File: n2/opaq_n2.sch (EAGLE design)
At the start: 40 parts, among them IC2 TS5A3157, IC3 ATSHA204_SOIC8, IC4 ACS712, IC5 ADS1100, IC6 ATMega-328, IC7 AT25F512BWIDE_5.3MM, IC8 LM2594HV, K1 62101021021, X1 16 MHz

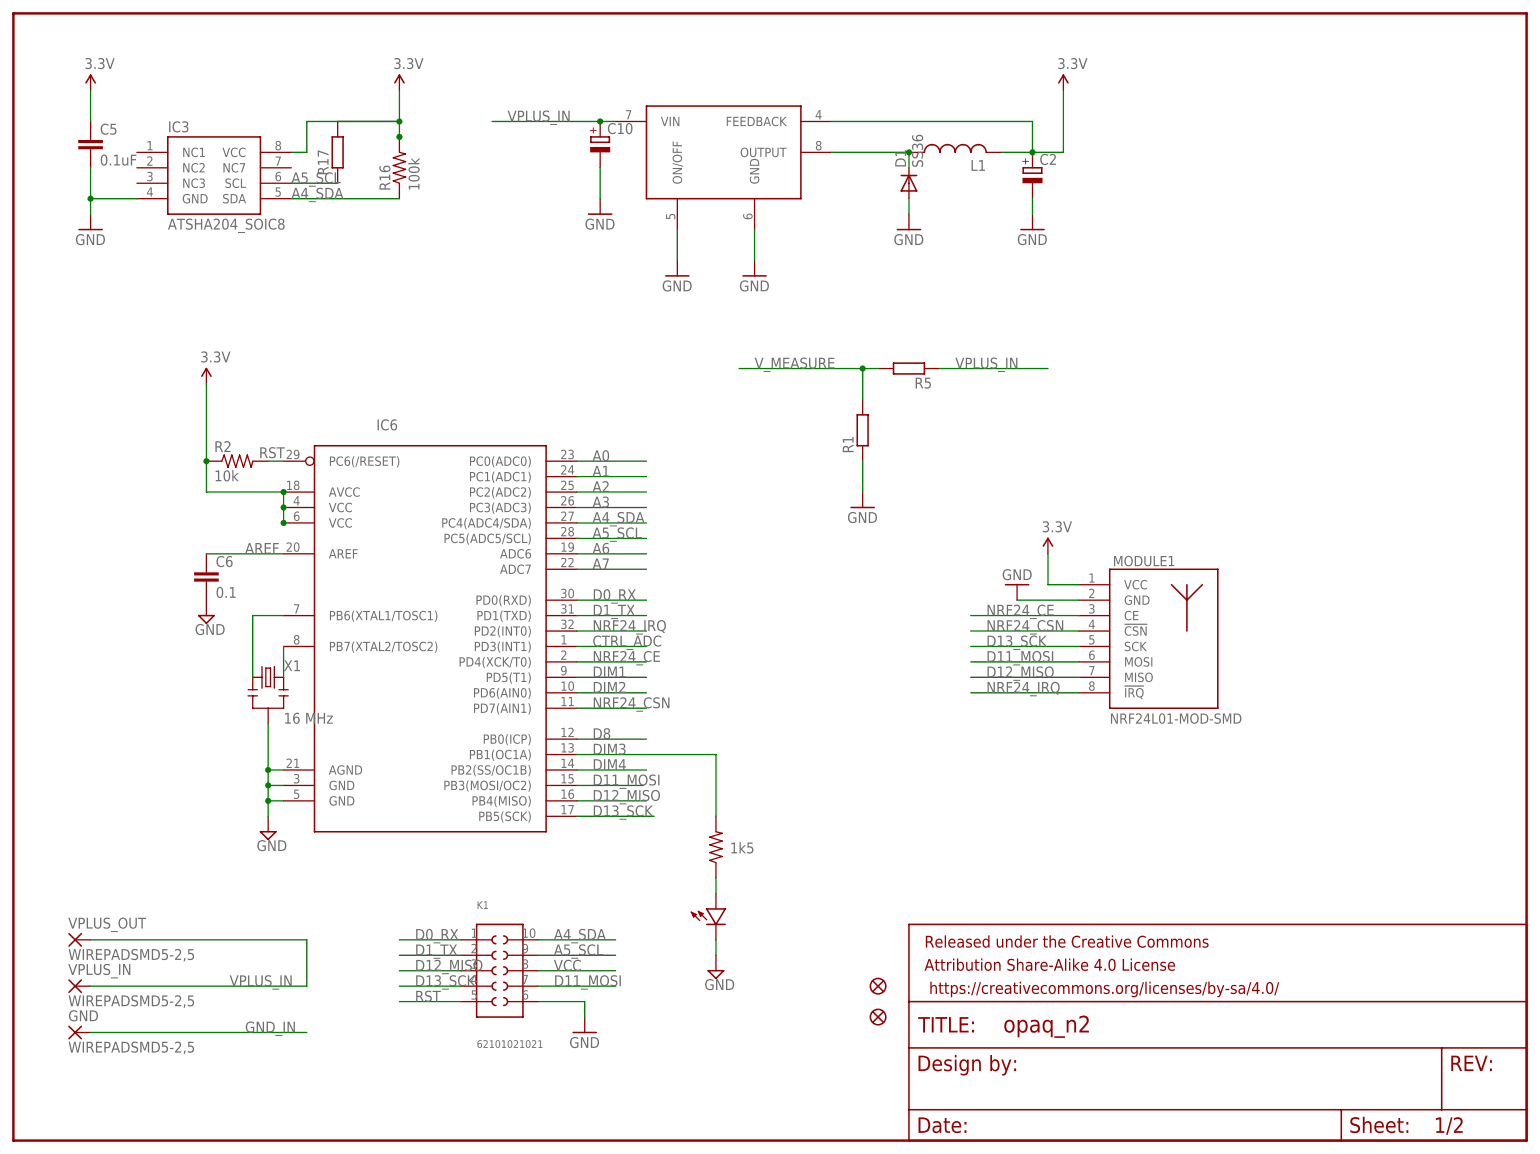
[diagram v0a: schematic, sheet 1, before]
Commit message: Updated opaq n2 hardware. Isolated power supply has been added.
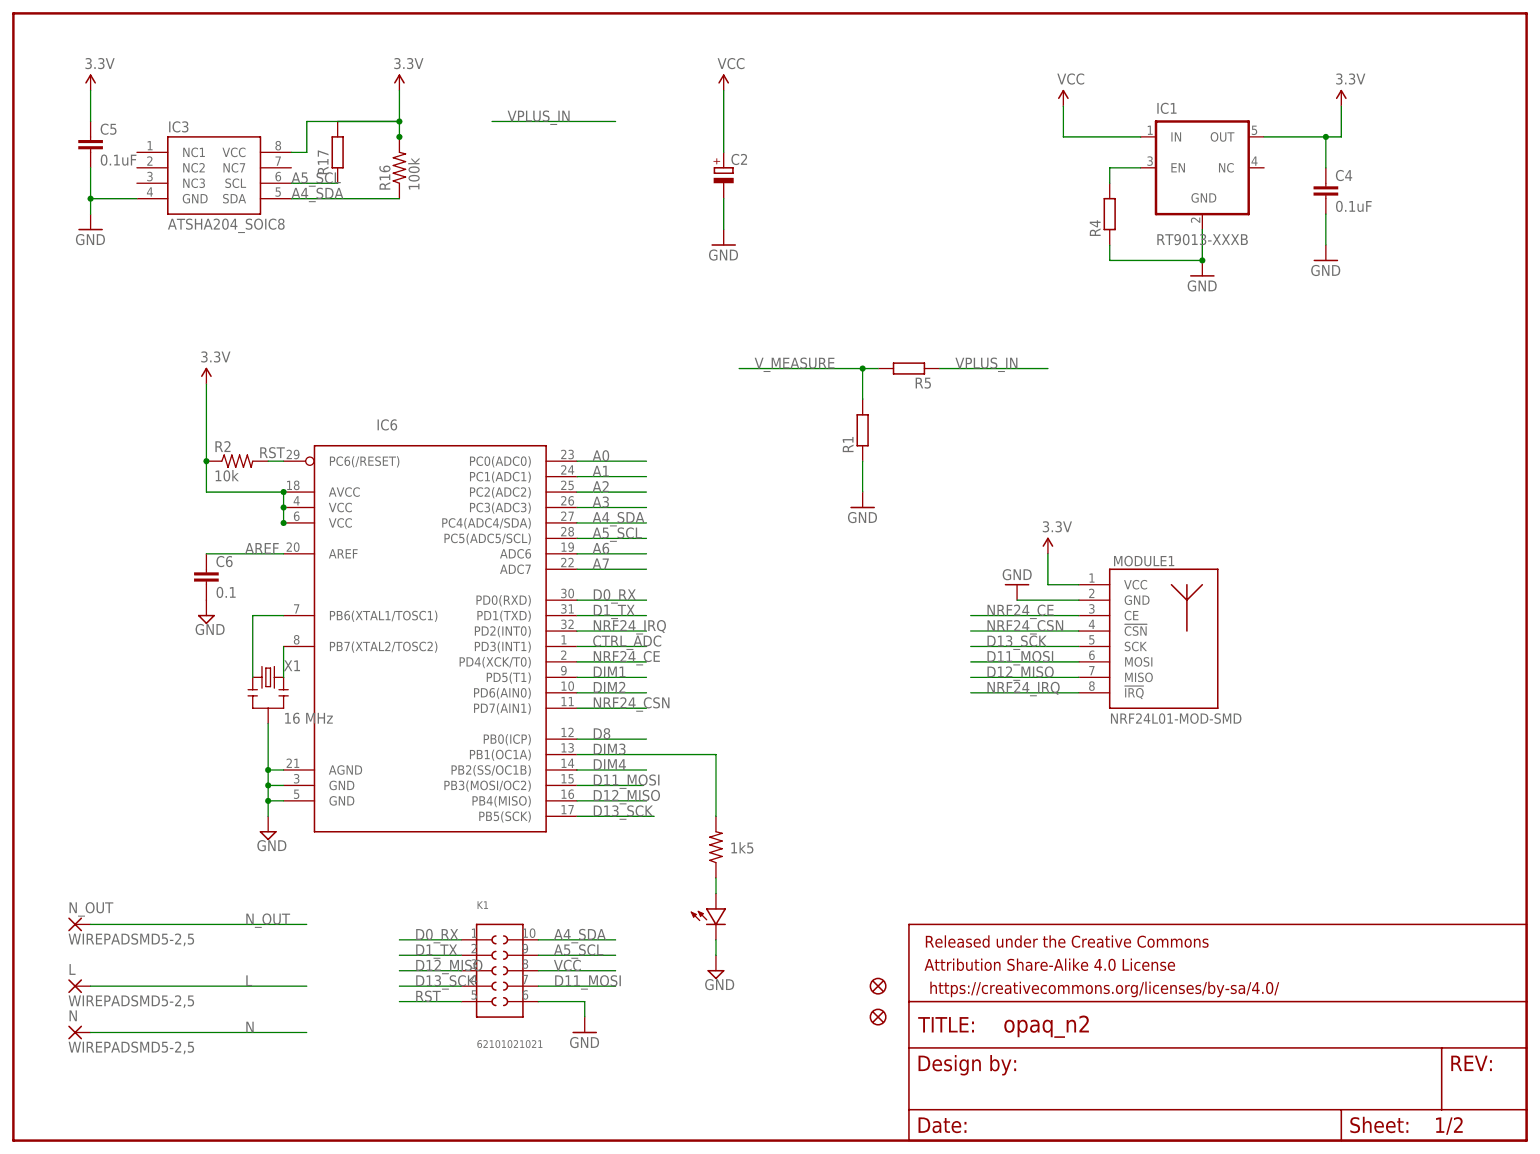
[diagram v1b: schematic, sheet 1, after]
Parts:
- removed C10: (no value), rcl:CPOL-EUD/7343-31R
- removed C8: (no value), resistor:C-EU225-062X268
- removed D1: SS36, SparkFun:DIODESMA
- removed D2, D3, D4, D5: (no value), adafruit:DIODESMA
- removed IC8: LM2594HV, apedro_lib:LM2594
- removed L1: (no value), apedro_lib:NR6045
- removed R6: (no value), resistor:R-EU_R2512W
- removed VPLUS_OUT: WIREPADSMD5-2,5, wirepad:WIREPADSMD5-2,5
- added 5V, L_IN, N_IN: MCS08, solpad:MCS08
- added C4: 0.1uF, SparkFun-Passives:CAP0805
- added IC1: RT9013-XXXB, v-reg_extra:RT9013-XXXB
- added N, N_OUT: WIREPADSMD5-2,5, wirepad:WIREPADSMD5-2,5
- added Q1: MMBT2222A, SparkFun-DiscreteSemi:TRANSISTOR_NPNMMBT2222A
- added R11, R4, R8: (no value), resistor:R-EU_R0805
- GND: value WIREPADSMD5-2,5 -> MCS08; device wirepad:WIREPADSMD5-2,5 -> solpad:MCS08
- renumbered VPLUS_IN to L
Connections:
- removed net GND_IN: GND.P, IC4.IP-@3, IC4.IP-@4
- removed net LC: C8.1, D2.C, D4.A, R6.1
- removed net N$17: D1.C, IC8.OUTPUT, L1.P$2
- removed net V+: D4.C, D5.C
- removed net V-: D2.A, D3.A
- new net N$10: IC1.EN, R4.2
- new net N_IN: IC4.IP-@3, IC4.IP-@4, U$1.NO1
- new net N_OUT: N_OUT.P, U$1.NO2
- new net RELAY_C: Q1.C, R8.2, U$1.COIL2
- new net RELAY_SET: Q1.B, R11.2
- net 3.3V: now also C4.1, IC1.OUT, R11.1; no longer C2.+, IC8.FEEDBACK, L1.P$1
- net GND: now also C4.2, GND.MP, IC1.GND, Q1.E, R4.1, U$1.COIL1; no longer C10.-, D1.A, IC4.IP+@1, IC4.IP+@2, IC8.GND, IC8.ON/OFF
- net L: now also L.P, L_IN.MP; no longer C8.2, R6.2
- net N: now also IC4.IP+@1, IC4.IP+@2, N.P, N_IN.MP; no longer D3.C, D5.A
- net VCC: now also 5V.MP, C2.+, IC1.IN, R8.1
- net VPLUS_IN: no longer C10.+, IC8.VIN, L.P, VPLUS_OUT.P
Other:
- moved on the sheet: C2

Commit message: Candidate version of opaq n2 for pcb production.
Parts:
- removed R8: (no value), resistor:R-EU_R0805
- added 7K471: (no value), ptc-ntc:B57164
- added CC: MCS08, solpad:MCS08
- added D1: tvs 5v, SparkFun:DIODESOD
- added D2: 1N4148, SparkFun:DIODESOD
- added D3: (no value), SparkFun:DIODESMB
- added R6, R7: (no value), resistor:R-EU_R0805
- added TRF250-300: (no value), fuse:TE5
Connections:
- removed net DIM1: IC6.PD5(T1)
- removed net L: L.P, L_IN.MP
- removed net RELAY_C: Q1.C, R8.2, U$1.COIL2
- new net CC: CC.MP, IC4.IP-@3, IC4.IP-@4
- new net CURRENT_VOUT5V: IC4.VOUT, R7.1
- new net LL: L.P, TRF250-300.1
- new net L_SAFE: 7K471.1, L_IN.MP
- new net N$3: 7K471.2, TRF250-300.2
- new net RELAY_GND: D2.A, Q1.C, U$1.COIL1
- net 3.3V: now also K1.8; no longer IC4.VCC
- net CURRENT_VOUT: now also R6.2, R7.2; no longer IC4.VOUT
- net GND: now also D1.A, D3.A, R6.1; no longer U$1.COIL1
- net N: no longer IC4.IP+@1, IC4.IP+@2
- net N_IN: now also IC4.IP+@1, IC4.IP+@2; no longer IC4.IP-@3, IC4.IP-@4
- net RELAY_SET: now also IC6.PD5(T1)
- net VCC: now also D1.C, D2.C, D3.C, IC4.VCC, U$1.COIL2; no longer K1.8, R8.1

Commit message: Opaq n2 hardware version r1.
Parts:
- removed CC: MCS08, solpad:MCS08
- added RLYIN: MCS08, solpad:MCS08
- renumbered N_OUT to RLYOUT
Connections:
- net CC: now also RLYIN.MP; no longer CC.MP
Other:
- moved on the sheet: 5V, GND, L_IN, N_IN
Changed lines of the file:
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@@
 <part name="R11" library="resistor" deviceset="R-EU_" device="R0805"/>
 <part name="P+21" library="SparkFun" deviceset="3.3V" device=""/>
-<part name="N_OUT" library="wirepad" deviceset="WIREPAD" device="SMD5-2,5"/>
+<part name="RLYOUT" library="wirepad" deviceset="WIREPAD" device="SMD5-2,5"/>
 <part name="GND" library="solpad" deviceset="MCS08" device=""/>
 <part name="5V" library="solpad" deviceset="MCS08" device=""/>
@@
 <part name="TRF250-300" library="fuse" deviceset="TE5" device=""/>
 <part name="L" library="wirepad" deviceset="WIREPAD" device="SMD5-2,5"/>
-<part name="CC" library="solpad" deviceset="MCS08" device=""/>
+<part name="RLYIN" library="solpad" deviceset="MCS08" device=""/>
 </parts>
 <sheets>
@@
 <instance part="C4" gate="G$1" x="215.9" y="154.94"/>
 <instance part="GND6" gate="1" x="215.9" y="144.78"/>
-<instance part="N_OUT" gate="G$1" x="10.16" y="35.56"/>
+<instance part="RLYOUT" gate="G$1" x="10.16" y="35.56"/>
 <instance part="P+13" gate="1" x="116.84" y="172.72"/>
 <instance part="P+3" gate="1" x="172.72" y="170.18"/>
@@
 <net name="N_OUT" class="0">
 <segment>
-<pinref part="N_OUT" gate="G$1" pin="P"/>
+<pinref part="RLYOUT" gate="G$1" pin="P"/>
 <wire x1="12.7" y1="35.56" x2="48.26" y2="35.56" width="0.1524" layer="91"/>
 <label x="38.1" y="35.56" size="1.778" layer="95"/>
@@
 <instance part="R11" gate="G$1" x="213.36" y="96.52" rot="R270"/>
 <instance part="P+21" gate="G$1" x="213.36" y="106.68"/>
-<instance part="GND" gate="G$1" x="109.22" y="116.84" rot="R90"/>
-<instance part="5V" gate="G$1" x="109.22" y="121.92" rot="R90"/>
-<instance part="N_IN" gate="G$1" x="109.22" y="132.08" rot="R90"/>
-<instance part="L_IN" gate="G$1" x="109.22" y="139.7" rot="R90"/>
+<instance part="GND" gate="G$1" x="25.4" y="7.62" rot="R90"/>
+<instance part="5V" gate="G$1" x="25.4" y="12.7" rot="R90"/>
+<instance part="N_IN" gate="G$1" x="25.4" y="22.86" rot="R90"/>
+<instance part="L_IN" gate="G$1" x="25.4" y="30.48" rot="R90"/>
 <instance part="P+6" gate="1" x="185.42" y="167.64"/>
 <instance part="R6" gate="G$1" x="226.06" y="134.62" rot="R90"/>
@@
 <instance part="GND9" gate="1" x="226.06" y="124.46"/>
 <instance part="D2" gate="G$1" x="170.18" y="73.66"/>
-<instance part="CC" gate="G$1" x="109.22" y="149.86" rot="R90"/>
+<instance part="RLYIN" gate="G$1" x="25.4" y="40.64" rot="R90"/>
 </instances>
 <busses>
@@
 <segment>
 <pinref part="GND" gate="G$1" pin="MP"/>
-<wire x1="111.76" y1="116.84" x2="137.16" y2="116.84" width="0.1524" layer="91"/>
-<label x="124.46" y="116.84" size="1.778" layer="95"/>
+<wire x1="27.94" y1="7.62" x2="53.34" y2="7.62" width="0.1524" layer="91"/>
+<label x="40.64" y="7.62" size="1.778" layer="95"/>
 </segment>
 <segment>
@@
 </segment>
 </net>
-<net name="V-" class="0">
-<segment>
-<wire x1="124.46" y1="93.98" x2="121.92" y2="93.98" width="0.1524" layer="91"/>
-<wire x1="121.92" y1="93.98" x2="121.92" y2="88.9" width="0.1524" layer="91"/>
-<wire x1="121.92" y1="88.9" x2="121.92" y2="86.36" width="0.1524" layer="91"/>
-<wire x1="121.92" y1="86.36" x2="124.46" y2="86.36" width="0.1524" layer="91"/>
-<wire x1="121.92" y1="88.9" x2="111.76" y2="88.9" width="0.1524" layer="91"/>
-<junction x="121.92" y="88.9"/>
-<label x="114.3" y="88.9" size="1.778" layer="95"/>
-</segment>
-</net>
-<net name="V+" class="0">
-<segment>
-<wire x1="142.24" y1="93.98" x2="144.78" y2="93.98" width="0.1524" layer="91"/>
-<wire x1="144.78" y1="93.98" x2="144.78" y2="88.9" width="0.1524" layer="91"/>
-<wire x1="144.78" y1="88.9" x2="144.78" y2="86.36" width="0.1524" layer="91"/>
-<wire x1="144.78" y1="86.36" x2="142.24" y2="86.36" width="0.1524" layer="91"/>
-<wire x1="144.78" y1="88.9" x2="154.94" y2="88.9" width="0.1524" layer="91"/>
-<junction x="144.78" y="88.9"/>
-<label x="147.32" y="88.9" size="1.778" layer="95"/>
-</segment>
-</net>
 <net name="N" class="0">
 <segment>
-<wire x1="137.16" y1="86.36" x2="132.08" y2="86.36" width="0.1524" layer="91"/>
-<wire x1="132.08" y1="86.36" x2="129.54" y2="86.36" width="0.1524" layer="91"/>
-<wire x1="132.08" y1="86.36" x2="132.08" y2="81.28" width="0.1524" layer="91"/>
-<junction x="132.08" y="86.36"/>
-<wire x1="132.08" y1="81.28" x2="119.38" y2="81.28" width="0.1524" layer="91"/>
-<label x="121.92" y="78.74" size="1.778" layer="95"/>
-</segment>
-<segment>
 <pinref part="N_IN" gate="G$1" pin="MP"/>
-<wire x1="111.76" y1="132.08" x2="137.16" y2="132.08" width="0.1524" layer="91"/>
-<label x="124.46" y="132.08" size="1.778" layer="95"/>
-</segment>
-</net>
-<net name="LC" class="0">
-<segment>
-<wire x1="129.54" y1="93.98" x2="132.08" y2="93.98" width="0.1524" layer="91"/>
-<wire x1="132.08" y1="93.98" x2="137.16" y2="93.98" width="0.1524" layer="91"/>
-<wire x1="132.08" y1="93.98" x2="132.08" y2="99.06" width="0.1524" layer="91"/>
-<junction x="132.08" y="93.98"/>
-<wire x1="132.08" y1="99.06" x2="119.38" y2="99.06" width="0.1524" layer="91"/>
-<label x="121.92" y="99.06" size="1.778" layer="95"/>
-</segment>
-<segment>
-<wire x1="111.76" y1="63.5" x2="121.92" y2="63.5" width="0.1524" layer="91"/>
-<label x="114.3" y="63.5" size="1.778" layer="95"/>
-</segment>
-</net>
-<net name="L" class="0">
-<segment>
-<wire x1="134.62" y1="63.5" x2="152.4" y2="63.5" width="0.1524" layer="91"/>
-<label x="147.32" y="63.5" size="1.778" layer="95"/>
+<wire x1="27.94" y1="22.86" x2="53.34" y2="22.86" width="0.1524" layer="91"/>
+<label x="40.64" y="22.86" size="1.778" layer="95"/>
 </segment>
 </net>
@@
 <segment>
 <pinref part="5V" gate="G$1" pin="MP"/>
-<wire x1="111.76" y1="121.92" x2="137.16" y2="121.92" width="0.1524" layer="91"/>
-<label x="124.46" y="121.92" size="1.778" layer="95"/>
+<wire x1="27.94" y1="12.7" x2="53.34" y2="12.7" width="0.1524" layer="91"/>
+<label x="40.64" y="12.7" size="1.778" layer="95"/>
 </segment>
 <segment>
@@
 <segment>
 <pinref part="L_IN" gate="G$1" pin="MP"/>
-<wire x1="111.76" y1="139.7" x2="137.16" y2="139.7" width="0.1524" layer="91"/>
-<label x="124.46" y="139.7" size="1.778" layer="95"/>
+<wire x1="27.94" y1="30.48" x2="53.34" y2="30.48" width="0.1524" layer="91"/>
+<label x="40.64" y="30.48" size="1.778" layer="95"/>
 </segment>
 </net>
 <net name="CC" class="0">
 <segment>
-<pinref part="CC" gate="G$1" pin="MP"/>
-<wire x1="111.76" y1="149.86" x2="137.16" y2="149.86" width="0.1524" layer="91"/>
-<label x="124.46" y="149.86" size="1.778" layer="95"/>
-</segment>
-<segment>
+<pinref part="RLYIN" gate="G$1" pin="MP"/>
+<wire x1="27.94" y1="40.64" x2="53.34" y2="40.64" width="0.1524" layer="91"/>
+<label x="40.64" y="40.64" size="1.778" layer="95"/>
+</segment>
+<segment>
